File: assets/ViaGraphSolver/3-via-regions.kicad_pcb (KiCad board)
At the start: 2 copper layers, 0 parts

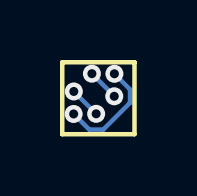
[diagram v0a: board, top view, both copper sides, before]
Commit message: Added Optimize 3 net Via Topology for  Improved Solve Performance
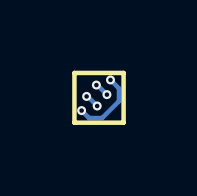
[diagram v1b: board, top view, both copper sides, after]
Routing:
- net net2: track 3.65 -> 2.41 mm
- net net3: track 1.06 -> 0.48 mm
- net net1: track 1.05 -> 0.48 mm
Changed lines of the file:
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@@
 	(net 3 "net3")
 	(gr_rect
-		(start -1.208638 -1.190738)
-		(end 1.199539 1.208373)
+		(start -0.802302 -0.833905)
+		(end 0.836522 0.823995)
 		(stroke
 			(width 0.15)
@@
 	)
 	(via
-		(at -0.82315 -0.216898)
-		(size 0.6)
-		(drill 0.3)
+		(at -0.396773 -0.05144)
+		(size 0.3)
+		(drill 0.15)
 		(layers "F.Cu" "B.Cu")
 		(free yes)
@@
 	)
 	(via
-		(at -0.078632 0.528441)
-		(size 0.6)
-		(drill 0.3)
+		(at -0.04486 0.267596)
+		(size 0.3)
+		(drill 0.15)
 		(layers "F.Cu" "B.Cu")
 		(free yes)
@@
 	)
 	(segment
-		(start -0.078632 0.528441)
-		(end -0.078632 0.52762)
+		(start -0.396773 -0.05144)
+		(end -0.363896 -0.05144)
 		(width 0.15)
 		(layer "B.Cu")
@@
 	)
 	(segment
-		(start -0.078632 0.52762)
-		(end -0.82315 -0.216898)
+		(start -0.363896 -0.05144)
+		(end -0.04486 0.267596)
 		(width 0.15)
 		(layer "B.Cu")
@@
 	)
 	(via
-		(at 0.529579 -0.806171)
-		(size 0.6)
-		(drill 0.3)
+		(at 0.39936 -0.600815)
+		(size 0.3)
+		(drill 0.15)
 		(layers "F.Cu" "B.Cu")
 		(free yes)
@@
 	)
 	(via
-		(at -0.82862 0.533085)
-		(size 0.6)
-		(drill 0.3)
+		(at -0.563329 0.420006)
+		(size 0.3)
+		(drill 0.15)
 		(layers "F.Cu" "B.Cu")
 		(free yes)
@@
 	)
 	(segment
-		(start 0.157885 1.054441)
-		(end 1.050634 0.161692)
+		(start 0.39936 -0.600815)
+		(end 0.681866 -0.318309)
 		(width 0.15)
 		(layer "B.Cu")
@@
 	)
 	(segment
-		(start -0.307264 1.054441)
-		(end 0.157885 1.054441)
+		(start 0.681866 -0.318309)
+		(end 0.681866 0.10797)
 		(width 0.15)
 		(layer "B.Cu")
@@
 	)
 	(segment
-		(start 1.050634 0.161692)
-		(end 1.050634 -0.285116)
+		(start -0.314739 0.668596)
+		(end -0.563329 0.420006)
 		(width 0.15)
 		(layer "B.Cu")
@@
 	)
 	(segment
-		(start 1.050634 -0.285116)
-		(end 0.529579 -0.806171)
+		(start 0.12124 0.668596)
+		(end -0.314739 0.668596)
 		(width 0.15)
 		(layer "B.Cu")
@@
 	)
 	(segment
-		(start -0.82862 0.533085)
-		(end -0.307264 1.054441)
+		(start 0.681866 0.10797)
+		(end 0.12124 0.668596)
 		(width 0.15)
 		(layer "B.Cu")
@@
 	)
 	(via
-		(at -0.220415 -0.809972)
-		(size 0.6)
-		(drill 0.3)
+		(at -0.070756 -0.430539)
+		(size 0.3)
+		(drill 0.15)
 		(layers "F.Cu" "B.Cu")
 		(free yes)
@@
 	)
 	(via
-		(at 0.524634 -0.056185)
-		(size 0.6)
-		(drill 0.3)
+		(at 0.280866 -0.111752)
+		(size 0.3)
+		(drill 0.15)
 		(layers "F.Cu" "B.Cu")
 		(free yes)
@@
 	)
 	(segment
-		(start 0.524634 -0.064923)
-		(end -0.220415 -0.809972)
+		(start -0.070756 -0.430539)
+		(end -0.037921 -0.430539)
 		(width 0.15)
 		(layer "B.Cu")
@@
 	)
 	(segment
-		(start 0.524634 -0.056185)
-		(end 0.524634 -0.064923)
+		(start -0.037921 -0.430539)
+		(end 0.280866 -0.111752)
 		(width 0.15)
 		(layer "B.Cu")
